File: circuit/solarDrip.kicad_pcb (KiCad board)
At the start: 2 copper layers, 39.5 x 40.7 mm, 16 parts, among them J1 DCDC_01x03_Socket, J2 MPPT_01x04_Pin, Q1 2N7002E, Q2 2N7002E, U1 ESP32-C3-WROOM-02

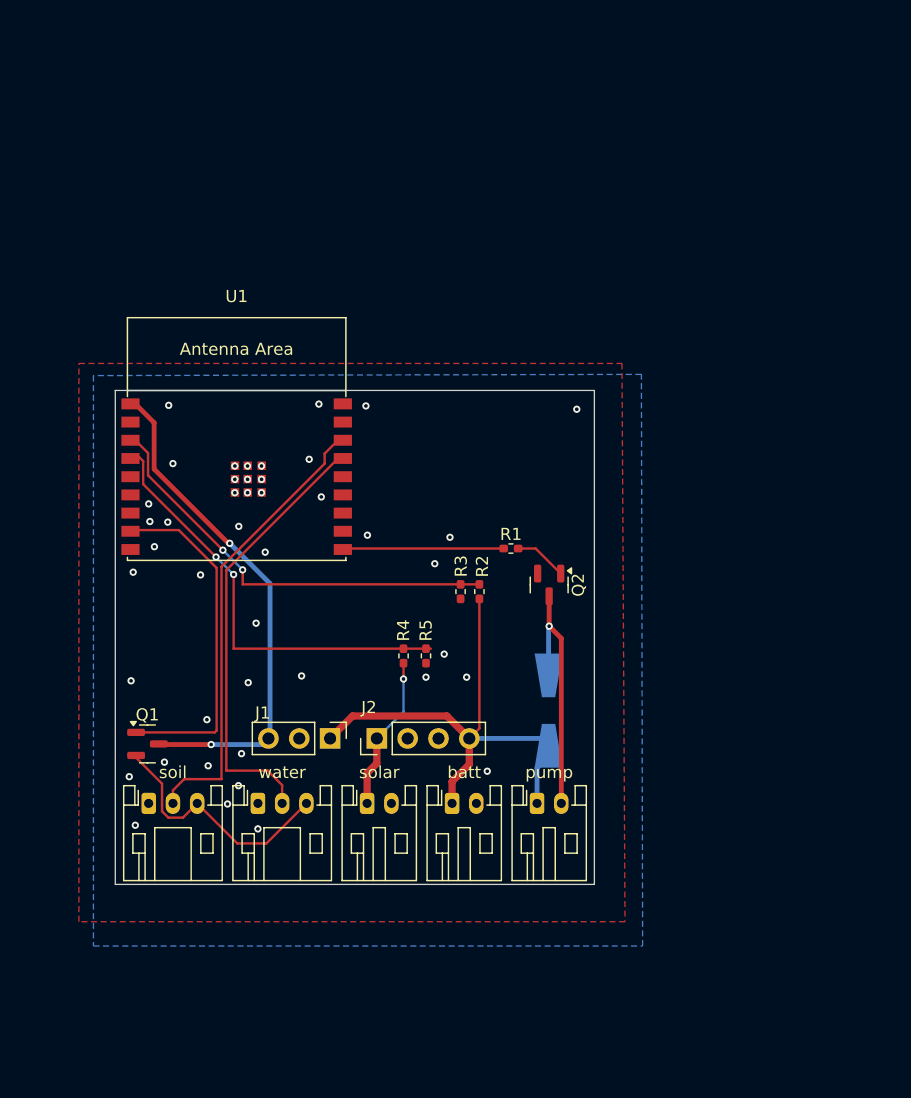
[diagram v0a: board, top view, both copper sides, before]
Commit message: prepare pcb for edge import
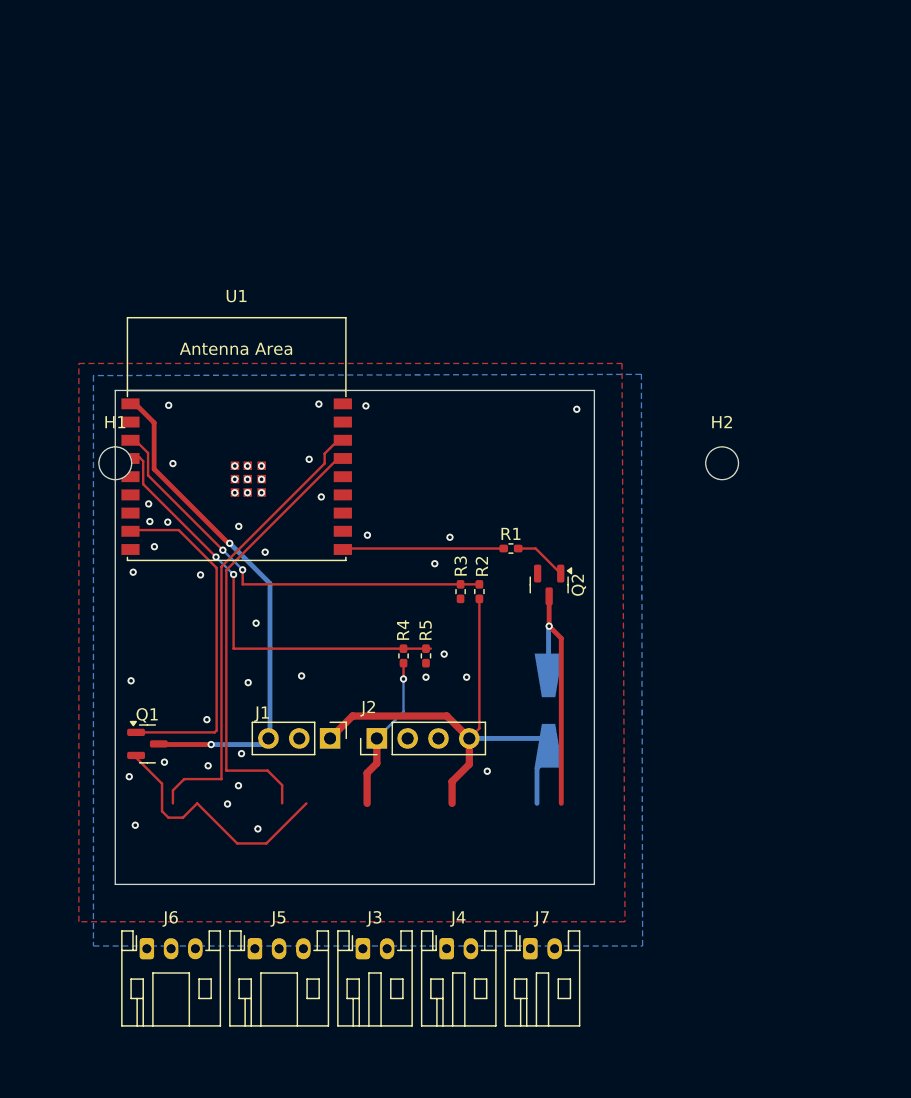
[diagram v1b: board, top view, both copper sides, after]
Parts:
- removed batt: battery, Connector_JST:JST_PH_S2B-PH-K_1x02_P2.00mm_Horizontal
- removed pump: pump, Connector_JST:JST_PH_S2B-PH-K_1x02_P2.00mm_Horizontal
- removed soil: soil_moisture, Connector_JST:JST_PH_S3B-PH-K_1x03_P2.00mm_Horizontal
- removed solar: solar_panel, Connector_JST:JST_PH_S2B-PH-K_1x02_P2.00mm_Horizontal
- removed water: water_level, Connector_JST:JST_PH_S3B-PH-K_1x03_P2.00mm_Horizontal
- added H1: MountingHole, MountingHole:MountingHole_2.7mm_M2.5_DIN965, F.Cu at (24.2, 42.0)
- added H2: MountingHole, MountingHole:MountingHole_2.7mm_M2.5_DIN965, F.Cu at (74.2, 42.0)
- added J3: solar_panel, Connector_JST:JST_PH_S2B-PH-K_1x02_P2.00mm_Horizontal, F.Cu at (44.6, 82.0)
- added J4: battery, Connector_JST:JST_PH_S2B-PH-K_1x02_P2.00mm_Horizontal, F.Cu at (51.5, 82.0)
- added J5: soil_moisture, Connector_JST:JST_PH_S3B-PH-K_1x03_P2.00mm_Horizontal, F.Cu at (35.8, 82.0)
- added J6: water_level, Connector_JST:JST_PH_S3B-PH-K_1x03_P2.00mm_Horizontal, F.Cu at (26.9, 82.0)
- added J7: pump, Connector_JST:JST_PH_S2B-PH-K_1x02_P2.00mm_Horizontal, F.Cu at (58.5, 82.0)
- R1: value 1K -> 100K
- R5: value 100K -> 1K
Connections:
- R1 pad 1: out_pump -> +5V
- R1 pad 2: Net-(Q2-G) -> solar_hi
- R2 pad 1: +3V8 -> solar_hi
- R2 pad 2: bat_hi -> GND
- R3 pad 1: bat_hi -> +3V8
- R3 pad 2: GND -> bat_hi
- R4 pad 1: +5V -> bat_hi
- R4 pad 2: solar_hi -> GND
- R5 pad 1: solar_hi -> out_pump
- R5 pad 2: GND -> Net-(Q2-G)

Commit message: add usb charging source
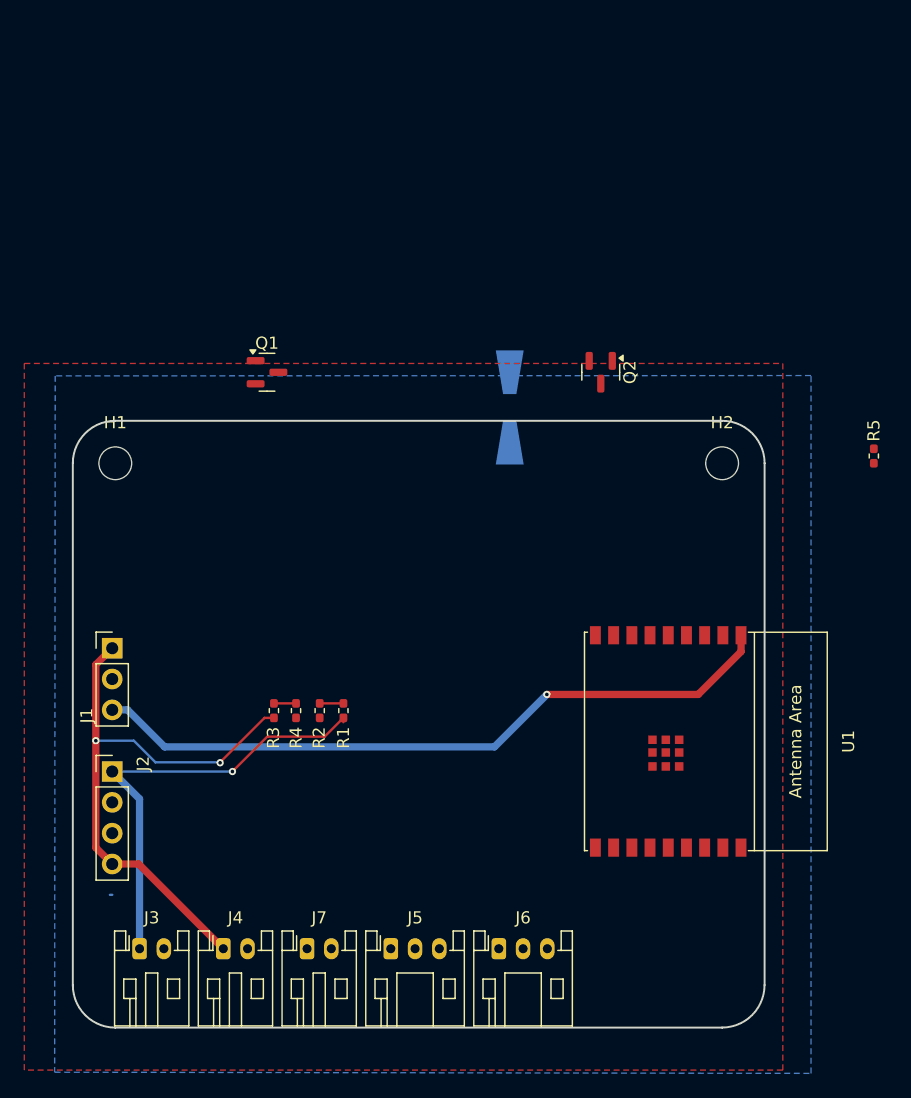
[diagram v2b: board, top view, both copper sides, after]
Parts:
- moved U1 41.9 mm to (69.9, 64.9), turned to -90 degrees
- moved R5 40.4 mm to (86.8, 41.4)
- moved Q1 32.2 mm to (36.8, 34.5)
- moved J6 29.0 mm to (55.9, 82.0)
- moved D1 25.2 mm to (56.8, 37.4)
- moved J2 22.0 mm to (24.0, 67.4), turned to 0 degrees
- moved J1 19.4 mm to (24.0, 57.2), turned to 0 degrees
- moved R1 19.2 mm to (43.0, 62.4), turned to 90 degrees
- moved J7 18.4 mm to (40.0, 82.0)
- moved J3 18.4 mm to (26.2, 82.0)
- moved J4 18.4 mm to (33.1, 82.0)
- moved R3 18.2 mm to (37.3, 62.4), turned to 90 degrees
- moved Q2 18.0 mm to (64.2, 34.5)
- moved R2 16.4 mm to (41.1, 62.4), turned to -90 degrees
- moved J5 11.2 mm to (47.0, 82.0)
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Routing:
- net in-a_moisture: track 37.8 -> 0.00 mm
- net in-a_water: track 36.6 -> 0.00 mm
- net solar_hi: track 36.0 -> 1.95 mm, vias 2 -> 0
- net bat_hi: track 35.5 -> 1.82 mm, vias 2 -> 0
- net out_sensors: track 28.5 -> 0.00 mm
- net +5V: track 12.8 -> 37.0 mm
- net pump_low: track 21.5 -> 0.00 mm, vias 1 -> 0
- net Net-(J5-Pin_3): track 20.8 -> 0.00 mm
- net +3V3: track 42.1 -> 57.7 mm, vias 2 -> 1
- net out_pump: track 13.3 -> 0.00 mm
- net +3V8: track 42.7 -> 47.9 mm, vias 0 -> 2
- net Net-(Q2-G): track 4.36 -> 0.00 mm
- net GND: vias 44 -> 0
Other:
- board size 39.5 x 40.7 mm -> 57 x 50 mm

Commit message: various updates
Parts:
- added D3: B130-E3, Diode_SMD:D_SMA, F.Cu at (45.8, 9.34)
- added J8: USB_C_Receptacle_USB2.0_14P, Connector_USB:USB_C_Receptacle_G-Switch_GT-USB-7010ASV, F.Cu at (36.2, 41.8)
- added Q3: FDN340P, Package_TO_SOT_SMD:SOT-23, F.Cu at (52.3, 9.46)
- added R6: 1K, Resistor_SMD:R_0402_1005Metric_Pad0.72x0.64mm_HandSolder, F.Cu at (47.7, 26.7)
- moved R5 28.8 mm to (62.6, 25.6)
- moved D1 25.8 mm to (37.2, 20.5)
- moved Q1 22.6 mm to (28.5, 13.5)
- moved Q2 18.3 mm to (55.3, 18.5)
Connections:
- net +3V3 renamed vcc_logic
- net +3V8 renamed vcc_battery
- net Net-(J5-Pin_3) renamed vcc_sensor_power
- J2 pad 1: +5V -> Net-(D3-K)
- J3 pad 1: +5V -> vcc_solar
- R1 pad 1: +5V -> vcc_solar
- U1 pad 13: unconnected-(U1-GPIO18/USB_D--Pad13) -> usb_d-
- U1 pad 14: unconnected-(U1-GPIO19/USB_D+-Pad14) -> usb_d+
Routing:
- net +5V: track 37.0 -> 0.00 mm, vias 1 -> 0
- net (no net): track 0.00 -> 37.0 mm, vias 0 -> 1

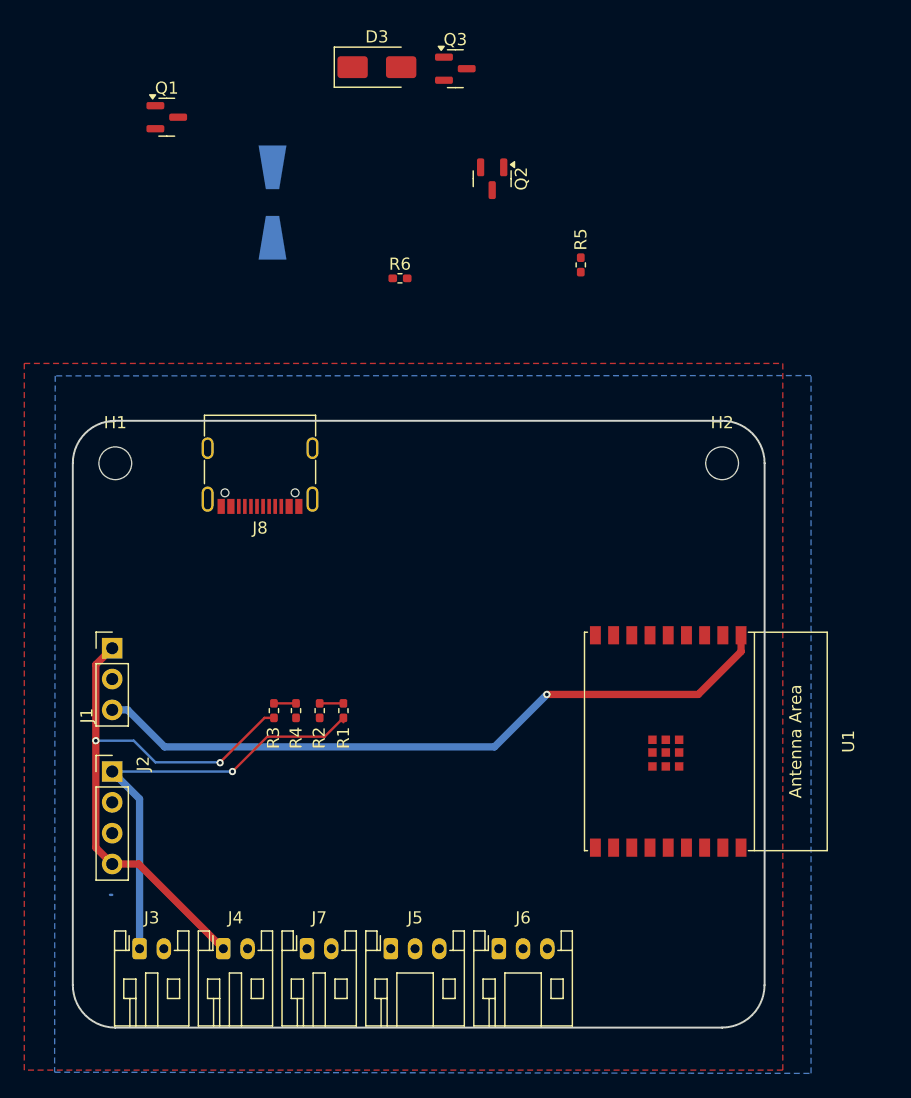
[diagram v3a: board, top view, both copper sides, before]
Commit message: init supermini variant
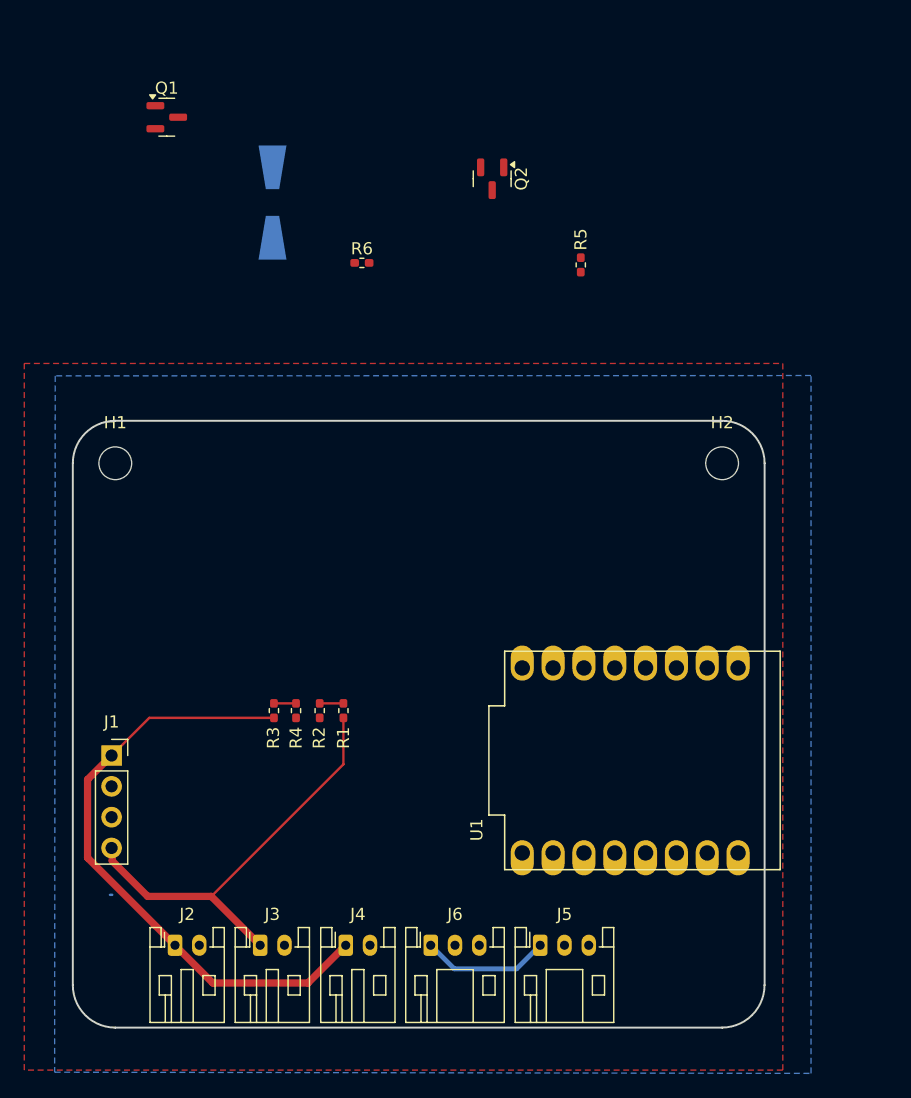
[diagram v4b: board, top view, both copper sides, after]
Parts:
- removed D3: B130-E3, Diode_SMD:D_SMA
- removed J7: pump, Connector_JST:JST_PH_S2B-PH-K_1x02_P2.00mm_Horizontal
- removed J8: USB_C_Receptacle_USB2.0_14P, Connector_USB:USB_C_Receptacle_G-Switch_GT-USB-7010ASV
- removed Q3: FDN340P, Package_TO_SOT_SMD:SOT-23
- D1: value M1 -> 1N4001
- J1: value DCDC_01x03_Socket -> solar_charger; footprint Connector_PinHeader_2.54mm:PinHeader_1x03_P2.54mm_Vertical -> Connector_PinSocket_2.54mm:PinSocket_1x04_P2.54mm_Vertical
- J2: value MPPT_01x04_Pin -> battery; footprint Connector_PinHeader_2.54mm:PinHeader_1x04_P2.54mm_Vertical -> Connector_JST:JST_PH_S2B-PH-K_1x02_P2.00mm_Horizontal
- J4: value battery -> pump
- Q1, Q2: value 2N7002E -> 2N7002K
- R1, R2, R3, R4: value 100K -> 10K
- R6: value 1K -> 100K
- U1: value ESP32-C3-WROOM-02 -> ESP32-C3_SUPERMINI; footprint espressiv_git:ESP32-C3-WROOM-02 -> supermini:MODULE_ESP32-C3_SUPERMINI
- moved J2 15.2 mm to (29.2, 81.7)
- moved J5 12.3 mm to (59.3, 81.7)
- moved J4 10.1 mm to (43.2, 81.7)
- moved J3 9.94 mm to (36.2, 81.7)
- moved J1 8.84 mm to (23.9, 66.1)
- moved J6 5.62 mm to (50.2, 81.7)
- moved R6 3.38 mm to (44.6, 25.5)
- moved U1 2.72 mm to (67.7, 66.5), turned to 90 degrees
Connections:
- J1 pad 3: vcc_logic -> GND
- J2 pad 1: Net-(D3-K) -> vcc_battery
- J4 pad 2: GND -> pump_low
- J5 pad 1: GND -> vcc_sensor_low
- J5 pad 3: vcc_sensor_power -> vcc_logic
- J6 pad 1: GND -> vcc_sensor_low
- J6 pad 3: vcc_sensor_power -> vcc_logic
- Q1 pad 2: vcc_sensor_power -> GND
- Q1 pad 3: vcc_logic -> vcc_sensor_low
- R6 pad 1: vcc_usb -> GND
- R6 pad 2: GND -> Net-(Q2-G)
- U1 pad 1: vcc_logic -> solar_hi
- U1 pad 2: unconnected-(U1-EN/CHIP_PU-Pad2) -> bat_hi
- U1 pad 3: bat_hi -> in-a_moisture
- U1 pad 4: solar_hi -> in-a_water
- U1 pad 7: unconnected-(U1-GPIO8-Pad7) -> out_sensors
- U1 pad 8: out_sensors -> scl
- U1 pad 9: GND -> sda
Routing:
- net vcc_logic: track 57.7 -> 0.00 mm, vias 1 -> 0
- net (no net): track 37.0 -> 0.19 mm, vias 1 -> 0
- net vcc_solar: track 0.00 -> 35.4 mm
- net vcc_sensor_low: track 0.00 -> 10.6 mm
- net vcc_battery: track 47.9 -> 50.7 mm, vias 2 -> 0

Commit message: first stab at pcb placement
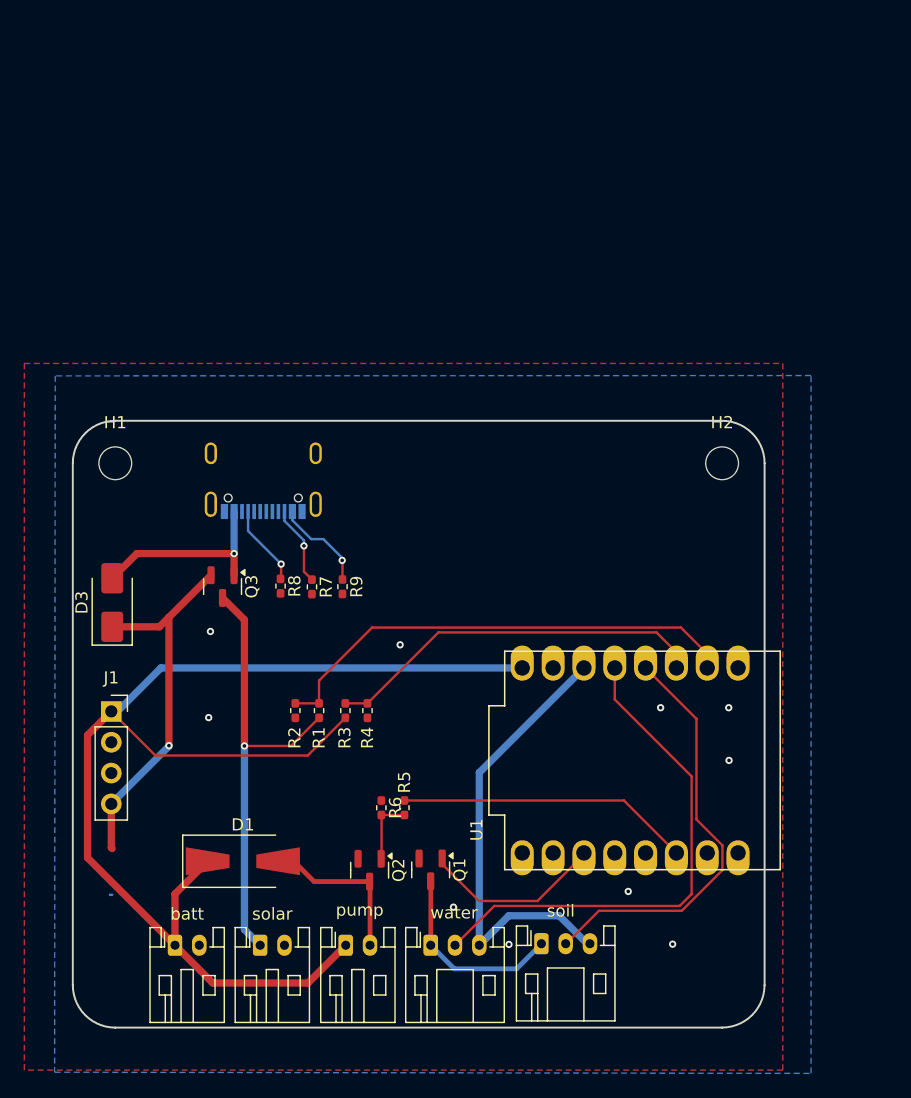
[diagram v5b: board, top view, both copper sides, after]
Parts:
- added D3: B130-E3, Diode_SMD:D_SMA, F.Cu at (24.0, 53.4)
- added J7: USB_C_Receptacle_USB2.0_14P, Connector_USB:USB_C_Receptacle_G-Switch_GT-USB-7010ASV, B.Cu at (36.4, 42.2)
- added Q3: FDN340P, Package_TO_SOT_SMD:SOT-23, F.Cu at (33.1, 52.1)
- added R7: 5k1, Resistor_SMD:R_0402_1005Metric_Pad0.72x0.64mm_HandSolder, F.Cu at (40.5, 52.2)
- added R8: 5k1, Resistor_SMD:R_0402_1005Metric_Pad0.72x0.64mm_HandSolder, F.Cu at (37.9, 52.1)
- added R9: 10K, Resistor_SMD:R_0402_1005Metric_Pad0.72x0.64mm_HandSolder, F.Cu at (43.0, 52.1)
- D1: moved to F.Cu
- J2: value battery -> batt
- J3: value solar_panel -> solar
- J5: value soil_moisture -> soil
- J6: value water_level -> water
- moved Q1 65.7 mm to (50.2, 75.5), turned to -90 degrees
- moved Q2 57.9 mm to (45.2, 75.5)
- moved D1 54.3 mm to (34.8, 74.8), turned to 0 degrees
- moved R5 47.0 mm to (48.1, 70.4)
- moved R6 44.9 mm to (46.2, 70.4), turned to -90 degrees
- moved R3 5.89 mm to (43.2, 62.4)
- moved R4 5.89 mm to (45.0, 62.4)
- moved J1 3.63 mm to (23.9, 62.4)
- moved R1 2.01 mm to (41.0, 62.4)
- moved R2 2.01 mm to (39.1, 62.4)
- moved J5 0.16 mm to (59.4, 81.6)
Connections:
- J1 pad 4: vcc_solar -> vcc_pwr
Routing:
- net vcc_battery: track 50.7 -> 105.2 mm
- net in-a_water: track 0.00 -> 42.5 mm
- net solar_hi: track 1.95 -> 39.7 mm
- net vcc_logic: track 0.00 -> 37.5 mm
- net in-a_moisture: track 0.00 -> 34.9 mm
- net vcc_pwr: track 0.00 -> 31.0 mm, vias 0 -> 1
- net bat_hi: track 1.82 -> 31.7 mm
- net out_pump: track 0.00 -> 24.2 mm
- net vcc_usb: track 0.00 -> 24.0 mm, vias 0 -> 2
- net out_sensors: track 0.00 -> 15.1 mm
- net pump_low: track 0.00 -> 13.5 mm
- net Net-(J7-CC1): track 0.00 -> 6.69 mm, vias 0 -> 1
- net Net-(J7-CC2): track 0.00 -> 6.55 mm, vias 0 -> 1
- net Net-(Q2-G): track 0.00 -> 5.54 mm
- net vcc_sensor_low: track 10.6 -> 15.9 mm
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
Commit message: routing done
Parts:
- moved U1 9.99 mm to (67.6, 56.5)
- moved J1 2.01 mm to (23.8, 64.4)
- moved D1 1.37 mm to (34.7, 76.1)
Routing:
- net vcc_logic: track 37.5 -> 47.5 mm
- net in-a_moisture: track 34.9 -> 40.7 mm
- net bat_hi: track 31.7 -> 37.2 mm
- net in-a_water: track 42.5 -> 47.2 mm
- net vcc_battery: track 105.2 -> 109.6 mm
- net out_pump: track 24.2 -> 27.2 mm
- net solar_hi: track 39.7 -> 42.0 mm
- net out_sensors: track 15.1 -> 16.0 mm
- net pump_low: track 13.5 -> 13.0 mm
- net GND: vias 10 -> 11
